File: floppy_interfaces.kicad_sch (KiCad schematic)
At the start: 24 parts, among them J13 Conn_01x04_Male, J14 Conn_02x17_Odd_Even, J16 Conn_01x04_Male, J6 SDF-60J for IEC 1541 serial p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, U22 74LS06N

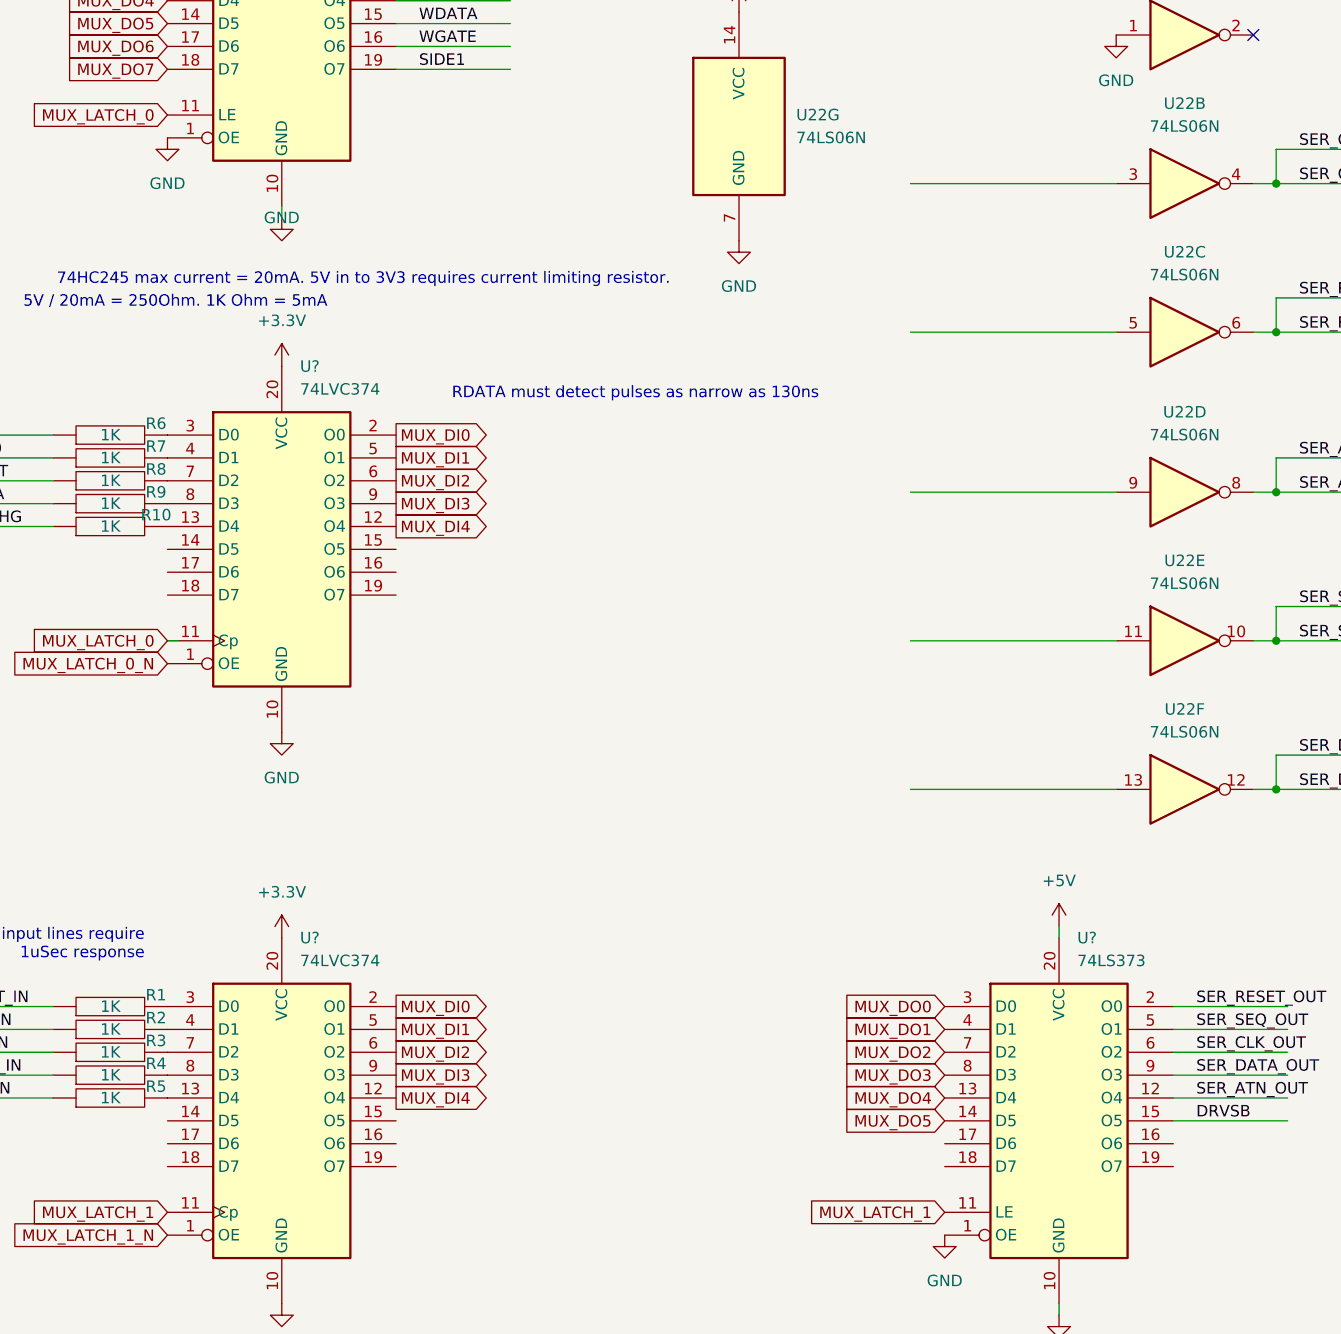
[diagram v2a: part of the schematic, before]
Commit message: connect missing IEC outputs
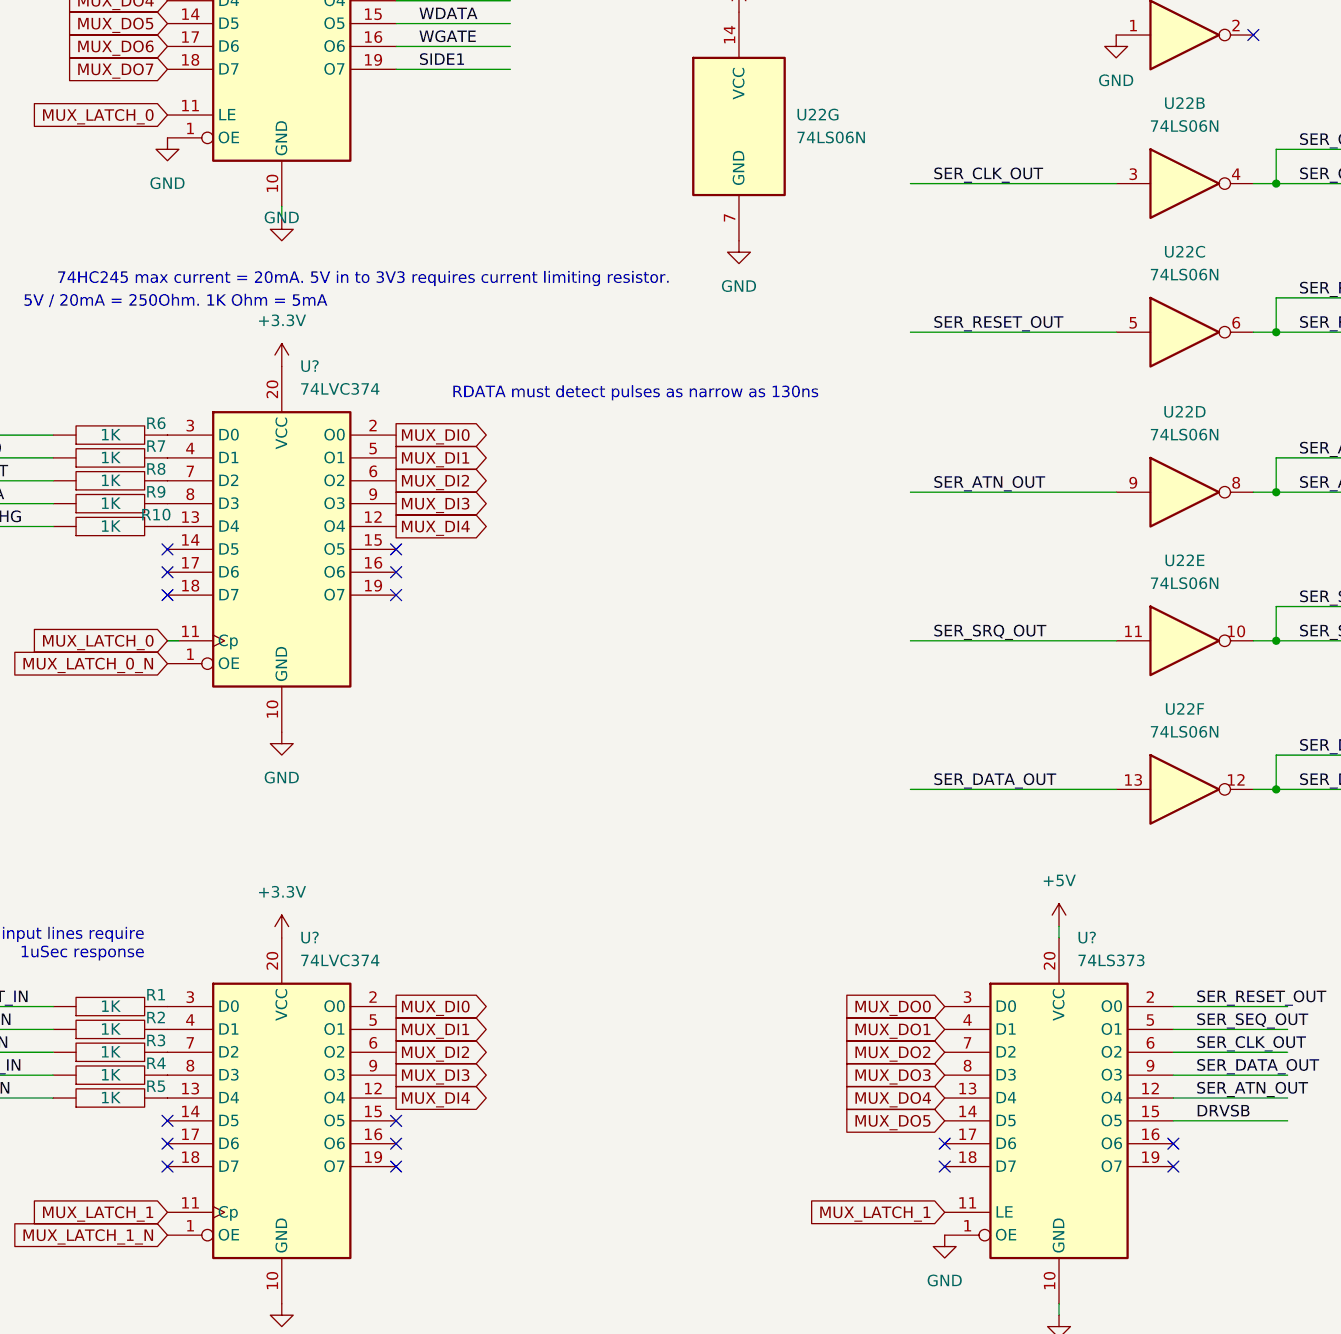
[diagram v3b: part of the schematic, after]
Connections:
- net SER_ATN_OUT: now also U22.9
- net SER_CLK_OUT: now also U22.3
- net SER_DATA_OUT: now also U22.13
- net SER_RESET_OUT: now also U22.5
- net SER_SRQ_OUT: now reaches U22.11
- no-connect marks 3 -> 19
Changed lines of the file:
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@@
   (junction (at 209.55 39.37) (diameter 0) (color 0 0 0 0)
   )
+  (no_connect (at 69.85 166.37))
   (no_connect (at 234.95 39.37))
+  (no_connect (at 156.21 171.45))
+  (no_connect (at 69.85 102.87))
+  (no_connect (at 130.81 168.91))
+  (no_connect (at 44.45 105.41))
+  (no_connect (at 44.45 171.45))
+  (no_connect (at 69.85 105.41))
+  (no_connect (at 44.45 102.87))
+  (no_connect (at 44.45 107.95))
+  (no_connect (at 130.81 171.45))
   (no_connect (at 234.95 41.91))
+  (no_connect (at 69.85 107.95))
+  (no_connect (at 44.45 168.91))
   (no_connect (at 165.1 45.72))
+  (no_connect (at 69.85 168.91))
+  (no_connect (at 69.85 171.45))
+  (no_connect (at 156.21 168.91))
+  (no_connect (at 44.45 166.37))
   (wire (pts (xy 167.64 58.42) (xy 181.61 58.42))
     (stroke (width 0) (type default) (color 0 0 0 0))
@@
     (effects (font (size 1.27 1.27)) (justify left bottom))
   )
+  (label "SER_ATN_OUT" (at 129.54 96.52 0)
+    (effects (font (size 1.27 1.27)) (justify left bottom))
+  )
   (label "RDATA" (at 226.06 72.39 0)
     (effects (font (size 1.27 1.27)) (justify left bottom))
@@
     (effects (font (size 1.27 1.27)) (justify left bottom))
   )
+  (label "SER_CLK_OUT" (at 129.54 62.23 0)
+    (effects (font (size 1.27 1.27)) (justify left bottom))
+  )
   (label "DRVSA" (at 226.06 52.07 0)
     (effects (font (size 1.27 1.27)) (justify left bottom))
@@
     (effects (font (size 1.27 1.27)) (justify left bottom))
   )
+  (label "SER_SRQ_OUT" (at 129.54 113.03 0)
+    (effects (font (size 1.27 1.27)) (justify left bottom))
+  )
   (label "DISKCHG" (at 20.32 100.33 0)
     (effects (font (size 1.27 1.27)) (justify left bottom))
@@
     (effects (font (size 1.27 1.27)) (justify left bottom))
   )
+  (label "SER_RESET_OUT" (at 129.54 78.74 0)
+    (effects (font (size 1.27 1.27)) (justify left bottom))
+  )
   (label "SER_DATA" (at 214.63 140.97 0)
     (effects (font (size 1.27 1.27)) (justify left bottom))
@@
     (effects (font (size 1.27 1.27)) (justify left bottom))
   )
+  (label "SER_DATA_OUT" (at 129.54 129.54 0)
+    (effects (font (size 1.27 1.27)) (justify left bottom))
+  )

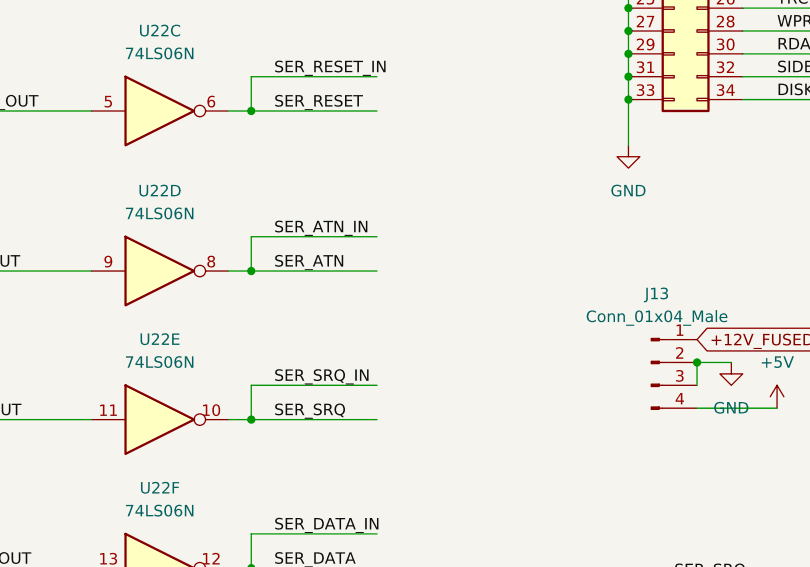
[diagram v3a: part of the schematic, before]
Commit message: setup pins on userport, but not yet connected to mux bus
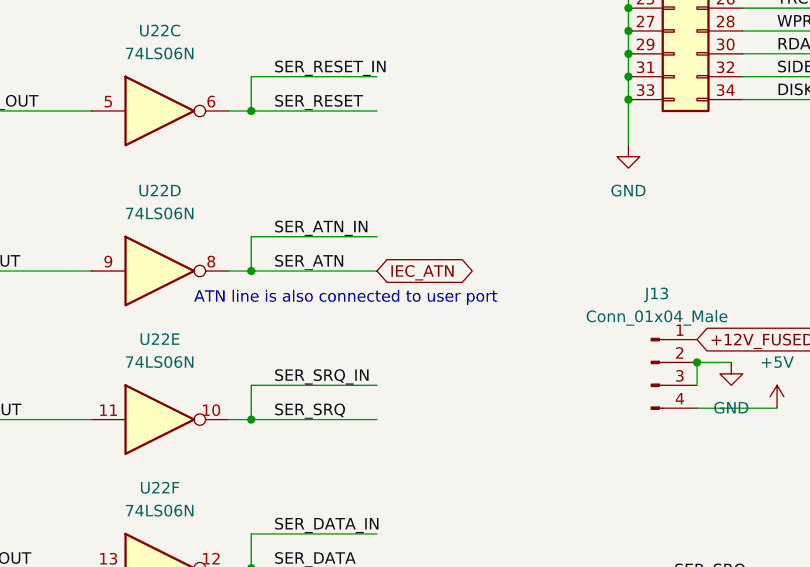
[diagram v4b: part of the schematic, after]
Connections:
- net SER_ATN renamed IEC_ATN
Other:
- note added: "ATN line is also connected to user port"
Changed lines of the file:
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@@
+    (effects (font (size 1.27 1.27)) (justify left bottom))
+  )
+  (text "ATN line is also connected to user port" (at 161.29 100.33 0)
     (effects (font (size 1.27 1.27)) (justify left bottom))
   )
@@
     )
   )
+  (global_label "IEC_ATN" (shape bidirectional) (at 181.61 96.52 0) (fields_autoplaced)
+    (effects (font (size 1.27 1.27)) (justify left))
+    (property "Intersheet References" "${INTERSHEET_REFS}" (id 0) (at 191.4012 96.4406 0)
+      (effects (font (size 1.27 1.27)) (justify left) hide)
+    )
+  )

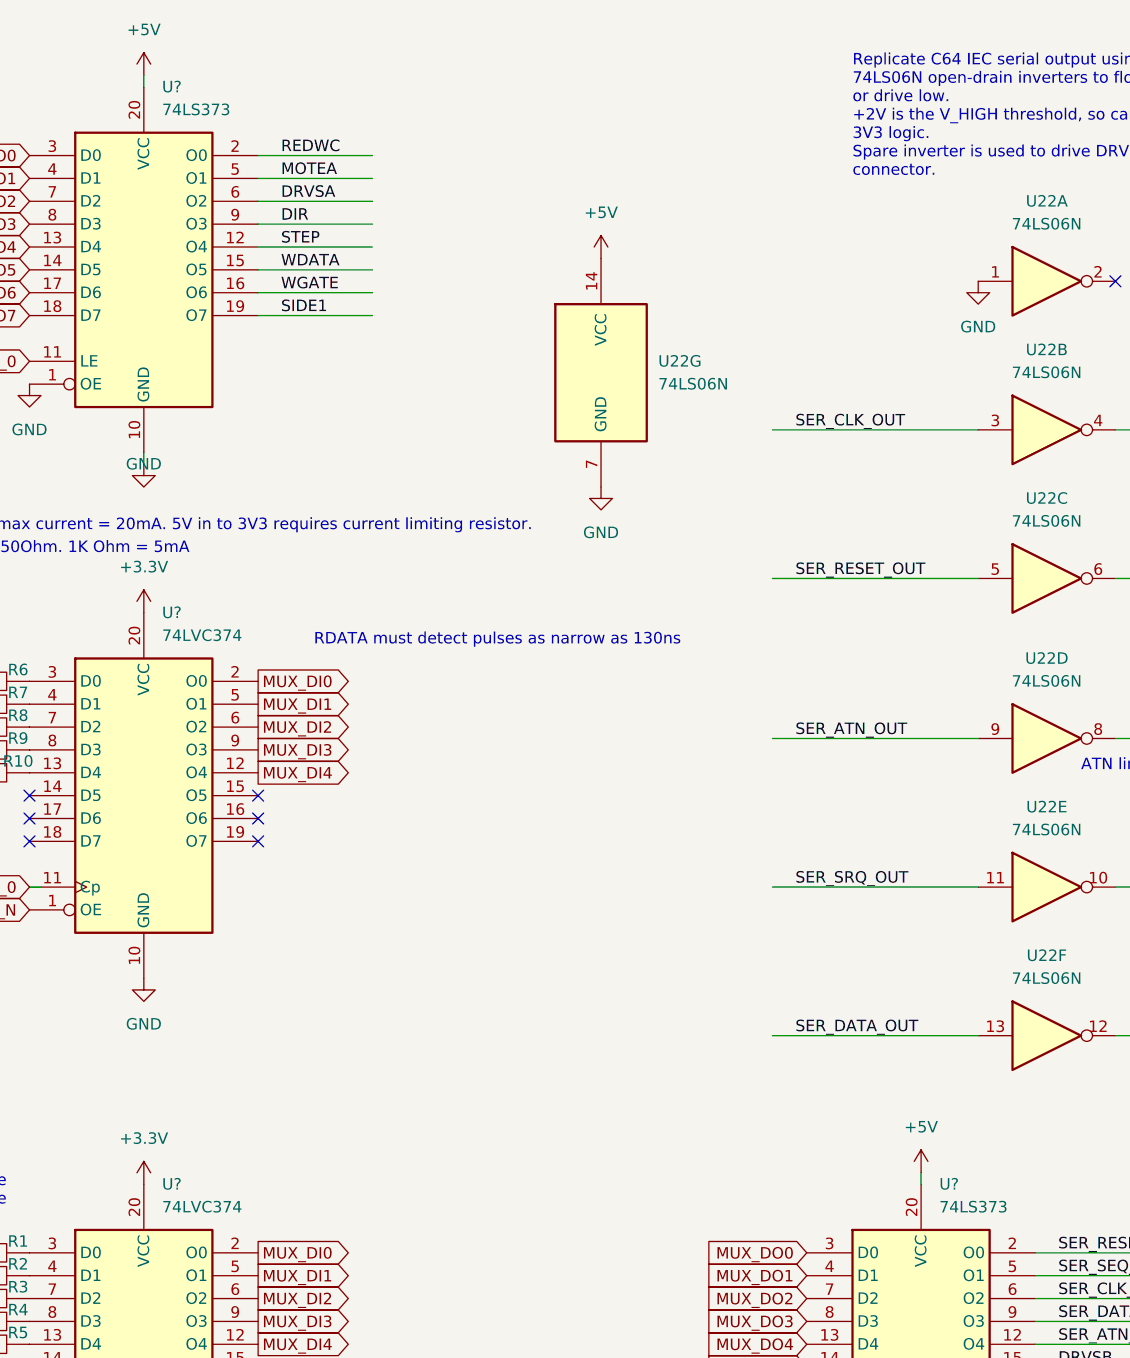
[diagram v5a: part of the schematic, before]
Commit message: add all missing footprints
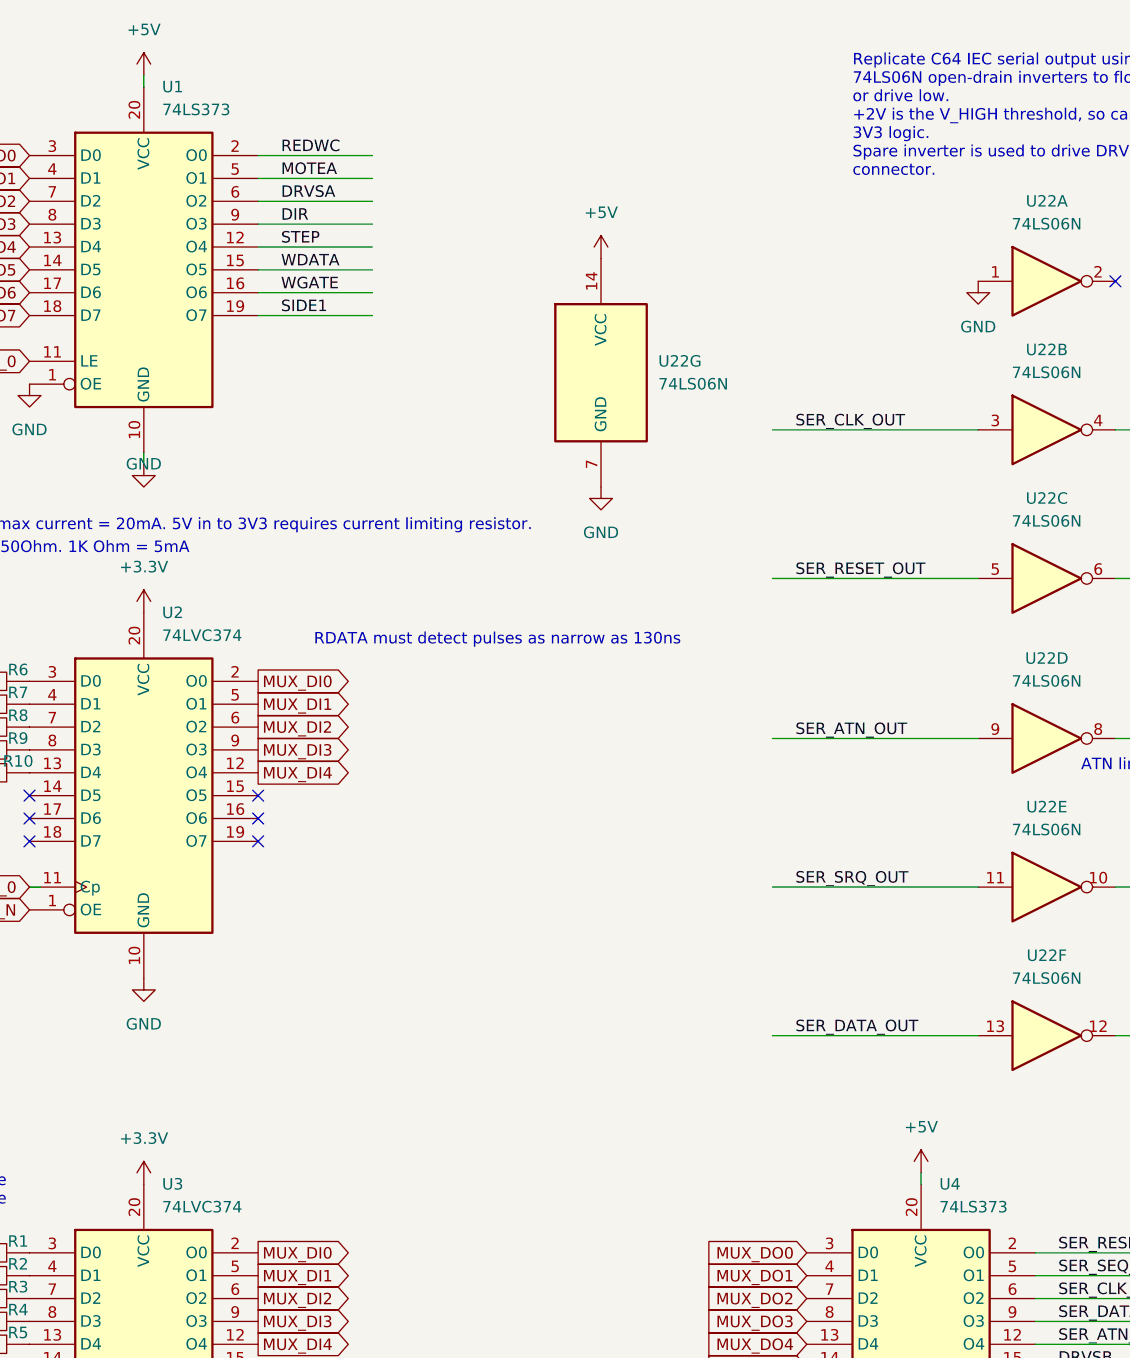
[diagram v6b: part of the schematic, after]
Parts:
- U1, U4: renamed from U?; footprint (none) -> Package_DIP:DIP-20_W7.62mm
- gave numbers to parts that had none: 2
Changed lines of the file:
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@@
   (symbol (lib_id "74xx:74LS373") (at 143.51 166.37 0) (unit 1)
     (in_bom yes) (on_board yes) (fields_autoplaced)
-    (property "Reference" "U?" (id 0) (at 145.5294 146.05 0)
+    (property "Reference" "U4" (id 0) (at 145.5294 146.05 0)
       (effects (font (size 1.27 1.27)) (justify left))
     )
@@
       (effects (font (size 1.27 1.27)) (justify left))
     )
-    (property "Footprint" "" (id 2) (at 143.51 166.37 0)
+    (property "Footprint" "Package_DIP:DIP-20_W7.62mm" (id 2) (at 143.51 166.37 0)
       (effects (font (size 1.27 1.27)) hide)
     )
@@
   (symbol (lib_id "power:GND") (at 130.81 179.07 0) (unit 1)
     (in_bom yes) (on_board yes) (fields_autoplaced)
-    (property "Reference" "#PWR?" (id 0) (at 130.81 185.42 0)
+    (property "Reference" "#PWR0108" (id 0) (at 130.81 185.42 0)
       (effects (font (size 1.27 1.27)) hide)
     )
@@
   (symbol (lib_id "74xx:74HC374") (at 57.15 166.37 0) (unit 1)
     (in_bom yes) (on_board yes) (fields_autoplaced)
-    (property "Reference" "U?" (id 0) (at 59.1694 146.05 0)
+    (property "Reference" "U3" (id 0) (at 59.1694 146.05 0)
       (effects (font (size 1.27 1.27)) (justify left))
     )
@@
   (symbol (lib_id "power:GND") (at 149.86 45.72 0) (unit 1)
     (in_bom yes) (on_board yes) (fields_autoplaced)
-    (property "Reference" "#PWR?" (id 0) (at 149.86 52.07 0)
+    (property "Reference" "#PWR0111" (id 0) (at 149.86 52.07 0)
       (effects (font (size 1.27 1.27)) hide)
     )
@@
   (symbol (lib_id "74xx:74HC374") (at 57.15 102.87 0) (unit 1)
     (in_bom yes) (on_board yes) (fields_autoplaced)
-    (property "Reference" "U?" (id 0) (at 59.1694 82.55 0)
+    (property "Reference" "U2" (id 0) (at 59.1694 82.55 0)
       (effects (font (size 1.27 1.27)) (justify left))
     )
@@
   (symbol (lib_id "power:GND") (at 143.51 187.96 0) (unit 1)
     (in_bom yes) (on_board yes) (fields_autoplaced)
-    (property "Reference" "#PWR?" (id 0) (at 143.51 194.31 0)
+    (property "Reference" "#PWR0117" (id 0) (at 143.51 194.31 0)
       (effects (font (size 1.27 1.27)) hide)
     )
@@
   (symbol (lib_id "power:+5V") (at 143.51 144.78 0) (unit 1)
     (in_bom yes) (on_board yes) (fields_autoplaced)
-    (property "Reference" "#PWR?" (id 0) (at 143.51 148.59 0)
+    (property "Reference" "#PWR0120" (id 0) (at 143.51 148.59 0)
       (effects (font (size 1.27 1.27)) hide)
     )
@@
   (symbol (lib_id "74xx:74LS373") (at 57.15 44.45 0) (unit 1)
     (in_bom yes) (on_board yes) (fields_autoplaced)
-    (property "Reference" "U?" (id 0) (at 59.1694 24.13 0)
+    (property "Reference" "U1" (id 0) (at 59.1694 24.13 0)
       (effects (font (size 1.27 1.27)) (justify left))
     )
@@
       (effects (font (size 1.27 1.27)) (justify left))
     )
-    (property "Footprint" "" (id 2) (at 57.15 44.45 0)
-      (effects (font (size 1.27 1.27)) hide)
-    )
+    (property "Footprint" "Package_DIP:DIP-20_W7.62mm" (id 2) (at 57.15 44.45 0)
+      (effects (font (size 1.27 1.27)) hide)
+    )
